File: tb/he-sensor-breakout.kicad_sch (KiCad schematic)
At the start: 22 parts, among them J1 Conn_01x01_Pin, J10 Conn_01x01_Pin, J11 Conn_01x01_Pin, J12 Conn_01x01_Pin, J13 Conn_01x01_Pin, J14 Conn_01x01_Pin, J2 Conn_01x01_Pin, J3 Conn_01x01_Pin, J4 Conn_01x01_Pin, J5 Conn_01x01_Pin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

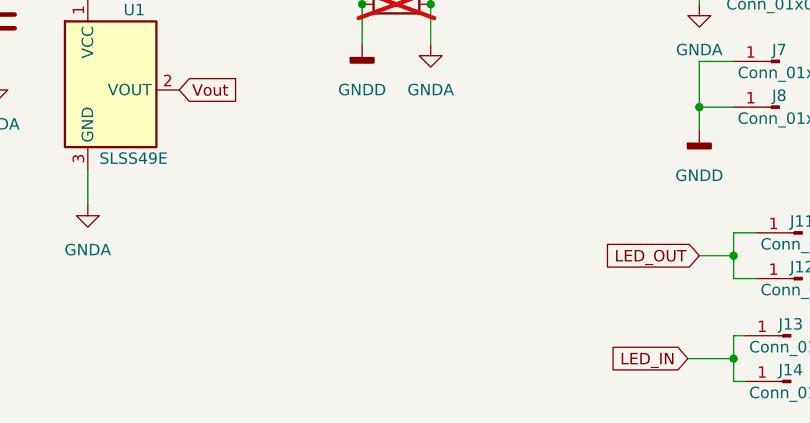
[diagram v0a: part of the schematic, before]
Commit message: adds vdd and vdd connection pads
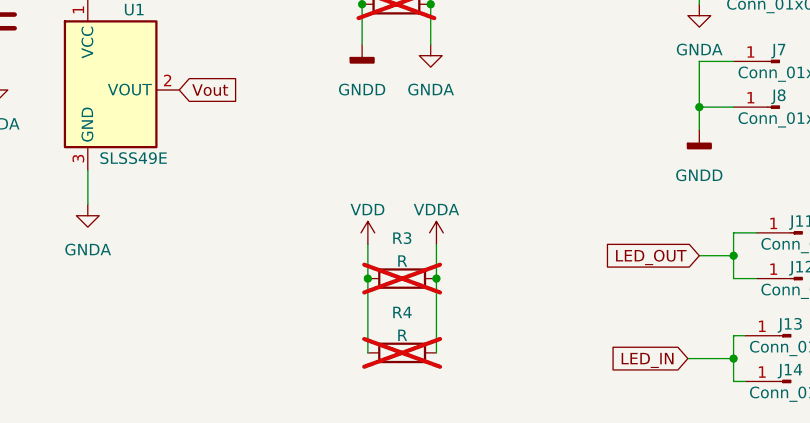
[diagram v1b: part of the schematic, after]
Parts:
- added R3, R4: R, Capacitor_SMD:C_0603_1608Metric, symbol Device:R
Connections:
- net VDD: now also R3.1, R4.1
- net VDDA: now also R3.2, R4.2
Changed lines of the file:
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@@
   (junction (at 240.03 77.47) (diameter 0) (color 0 0 0 0)
   )
+  (junction (at 152.4 106.68) (diameter 0) (color 0 0 0 0)
+  )
   (junction (at 144.145 76.2) (diameter 0) (color 0 0 0 0)
   )
+  (junction (at 144.78 106.68) (diameter 0) (color 0 0 0 0)
+  )
   (junction (at 185.42 115.57) (diameter 0) (color 0 0 0 0)
   )
@@
     (stroke (width 0) (type default))
   )
+  (wire (pts (xy 144.78 102.87) (xy 144.78 106.68))
+    (stroke (width 0) (type default))
+  )
   (wire (pts (xy 240.03 58.42) (xy 240.03 60.96))
     (stroke (width 0) (type default))
@@
     (stroke (width 0) (type default))
   )
+  (wire (pts (xy 152.4 106.68) (xy 152.4 114.935))
+    (stroke (width 0) (type default))
+  )
   (wire (pts (xy 240.03 74.93) (xy 240.03 77.47))
     (stroke (width 0) (type default))
@@
     (stroke (width 0) (type default))
   )
+  (wire (pts (xy 144.78 106.68) (xy 144.78 114.935))
+    (stroke (width 0) (type default))
+  )
   (wire (pts (xy 91.44 71.755) (xy 91.44 74.295))
     (stroke (width 0) (type default))
@@
   )
   (wire (pts (xy 185.42 101.6) (xy 187.96 101.6))
+    (stroke (width 0) (type default))
+  )
+  (wire (pts (xy 152.4 102.87) (xy 152.4 106.68))
     (stroke (width 0) (type default))
   )
@@
     )
   )
+  (symbol (lib_id "power:VDD") (at 144.78 102.87 0) (unit 1)
+    (in_bom yes) (on_board yes) (dnp no) (fields_autoplaced)
+    (property "Reference" "#PWR016" (at 144.78 106.68 0)
+      (effects (font (size 1.27 1.27)) hide)
+    )
+    (property "Value" "VDD" (at 144.78 99.06 0)
+      (effects (font (size 1.27 1.27)))
+    )
+    (property "Footprint" "" (at 144.78 102.87 0)
+      (effects (font (size 1.27 1.27)) hide)
+    )
+    (property "Datasheet" "" (at 144.78 102.87 0)
+      (effects (font (size 1.27 1.27)) hide)
+    )
+    (pin "1")
+    (instances
+      (project "he-sensor-breakout"
+        (path "/1c4931b8-ce31-46e7-81b2-9cf79bd80c14"
+          (reference "#PWR016") (unit 1)
+        )
+      )
+    )
+  )
   (symbol (lib_id "Connector:Conn_01x01_Pin") (at 193.04 106.68 180) (unit 1)
     (in_bom yes) (on_board yes) (dnp no)
@@
         (path "/1c4931b8-ce31-46e7-81b2-9cf79bd80c14"
           (reference "J14") (unit 1)
+        )
+      )
+    )
+  )
+  (symbol (lib_id "Device:R") (at 148.59 114.935 90) (unit 1)
+    (in_bom yes) (on_board yes) (dnp yes) (fields_autoplaced)
+    (property "Reference" "R4" (at 148.59 110.49 90)
+      (effects (font (size 1.27 1.27)))
+    )
+    (property "Value" "R" (at 148.59 113.03 90)
+      (effects (font (size 1.27 1.27)))
+    )
+    (property "Footprint" "Capacitor_SMD:C_0603_1608Metric" (at 148.59 116.713 90)
+      (effects (font (size 1.27 1.27)) hide)
+    )
+    (property "Datasheet" "~" (at 148.59 114.935 0)
+      (effects (font (size 1.27 1.27)) hide)
+    )
+    (pin "1")
+    (pin "2")
+    (instances
+      (project "he-sensor-breakout"
+        (path "/1c4931b8-ce31-46e7-81b2-9cf79bd80c14"
+          (reference "R4") (unit 1)
         )
       )
@@
     )
   )
+  (symbol (lib_id "Device:R") (at 148.59 106.68 90) (unit 1)
+    (in_bom yes) (on_board yes) (dnp yes) (fields_autoplaced)
+    (property "Reference" "R3" (at 148.59 102.235 90)
+      (effects (font (size 1.27 1.27)))
+    )
+    (property "Value" "R" (at 148.59 104.775 90)
+      (effects (font (size 1.27 1.27)))
+    )
+    (property "Footprint" "Capacitor_SMD:C_0603_1608Metric" (at 148.59 108.458 90)
+      (effects (font (size 1.27 1.27)) hide)
+    )
+    (property "Datasheet" "~" (at 148.59 106.68 0)
+      (effects (font (size 1.27 1.27)) hide)
+    )
+    (pin "1")
+    (pin "2")
+    (instances
+      (project "he-sensor-breakout"
+        (path "/1c4931b8-ce31-46e7-81b2-9cf79bd80c14"
+          (reference "R3") (unit 1)
+        )
+      )
+    )
+  )
   (symbol (lib_id "power:GNDA") (at 103.505 84.455 0) (unit 1)
     (in_bom yes) (on_board yes) (dnp no) (fields_autoplaced)
@@
         )
       )
+    )
+  )
+  (symbol (lib_id "power:VDDA") (at 152.4 102.87 0) (unit 1)
+    (in_bom yes) (on_board yes) (dnp no) (fields_autoplaced)
+    (property "Reference" "#PWR015" (at 152.4 106.68 0)
+      (effects (font (size 1.27 1.27)) hide)
+    )
+    (property "Value" "VDDA" (at 152.4 99.06 0)
+      (effects (font (size 1.27 1.27)))
+    )
+    (property "Footprint" "" (at 152.4 102.87 0)
+      (effects (font (size 1.27 1.27)) hide)
+    )
+    (property "Datasheet" "" (at 152.4 102.87 0)
+      (effects (font (size 1.27 1.27)) hide)
+    )
+    (pin "1")
+    (instances
+      (project "he-sensor-breakout"
+        (path "/1c4931b8-ce31-46e7-81b2-9cf79bd80c14"
+          (reference "#PWR015") (unit 1)
+        )
+      )

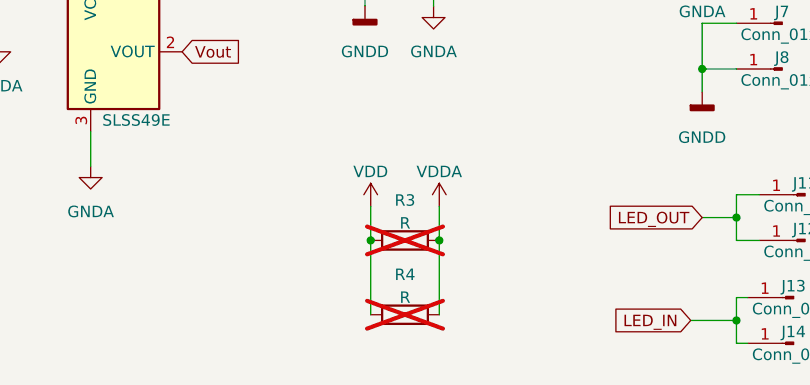
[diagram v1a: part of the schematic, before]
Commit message: vdda and vdd connection
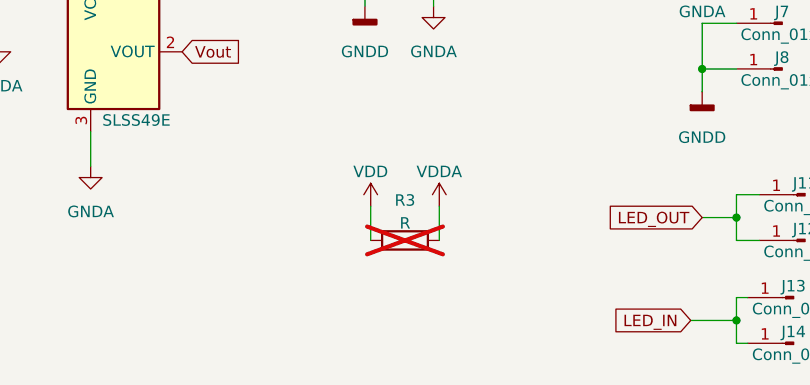
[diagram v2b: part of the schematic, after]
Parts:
- removed R4: R, Capacitor_SMD:C_0603_1608Metric, symbol Device:R
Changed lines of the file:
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@@
   (junction (at 240.03 77.47) (diameter 0) (color 0 0 0 0)
   )
-  (junction (at 152.4 106.68) (diameter 0) (color 0 0 0 0)
-  )
   (junction (at 144.145 76.2) (diameter 0) (color 0 0 0 0)
   )
-  (junction (at 144.78 106.68) (diameter 0) (color 0 0 0 0)
-  )
   (junction (at 185.42 115.57) (diameter 0) (color 0 0 0 0)
   )
@@
     (stroke (width 0) (type default))
   )
-  (wire (pts (xy 152.4 106.68) (xy 152.4 114.935))
-    (stroke (width 0) (type default))
-  )
   (wire (pts (xy 240.03 74.93) (xy 240.03 77.47))
     (stroke (width 0) (type default))
@@
   )
   (wire (pts (xy 181.61 69.85) (xy 181.61 74.93))
-    (stroke (width 0) (type default))
-  )
-  (wire (pts (xy 144.78 106.68) (xy 144.78 114.935))
     (stroke (width 0) (type default))
   )
@@
         )
       )
-    )
-  )
-  (symbol (lib_id "Device:R") (at 148.59 114.935 90) (unit 1)
-    (in_bom yes) (on_board yes) (dnp yes) (fields_autoplaced)
-    (property "Reference" "R4" (at 148.59 110.49 90)
-      (effects (font (size 1.27 1.27)))
-    )
-    (property "Value" "R" (at 148.59 113.03 90)
-      (effects (font (size 1.27 1.27)))
-    )
-    (property "Footprint" "Capacitor_SMD:C_0603_1608Metric" (at 148.59 116.713 90)
-      (effects (font (size 1.27 1.27)) hide)
-    )
-    (property "Datasheet" "~" (at 148.59 114.935 0)
-      (effects (font (size 1.27 1.27)) hide)
-    )
-    (pin "1")
-    (pin "2")
-    (instances
-      (project "he-sensor-breakout"
-        (path "/1c4931b8-ce31-46e7-81b2-9cf79bd80c14"
-          (reference "R4") (unit 1)
-        )
-      )

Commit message: moves GND shorts
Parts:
- R1, R2, R3: footprint Capacitor_SMD:C_0603_1608Metric -> Resistor_SMD:R_0402_1005Metric_Pad0.72x0.64mm_HandSolder
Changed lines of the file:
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@@
       (effects (font (size 1.27 1.27)))
     )
-    (property "Footprint" "Capacitor_SMD:C_0603_1608Metric" (at 147.955 69.723 90)
+    (property "Footprint" "Resistor_SMD:R_0402_1005Metric_Pad0.72x0.64mm_HandSolder" (at 147.955 69.723 90)
       (effects (font (size 1.27 1.27)) hide)
     )
@@
       (effects (font (size 1.27 1.27)))
     )
-    (property "Footprint" "Capacitor_SMD:C_0603_1608Metric" (at 147.955 77.978 90)
+    (property "Footprint" "Resistor_SMD:R_0402_1005Metric_Pad0.72x0.64mm_HandSolder" (at 147.955 77.978 90)
       (effects (font (size 1.27 1.27)) hide)
     )
@@
       (effects (font (size 1.27 1.27)))
     )
-    (property "Footprint" "Capacitor_SMD:C_0603_1608Metric" (at 148.59 108.458 90)
-      (effects (font (size 1.27 1.27)) hide)
-    )
+    (property "Footprint" "Resistor_SMD:R_0402_1005Metric_Pad0.72x0.64mm_HandSolder" (at 148.59 108.458 90)
+      (effects (font (size 1.27 1.27)) hide)
+    )
